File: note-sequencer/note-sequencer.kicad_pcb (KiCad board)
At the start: 2 copper layers, 160.9 x 383.9 mm, 132 parts, among them J1 Pitch, J10 Gate, J11 Velocity, J12 Clock, J13 LED Socket, J14 Conn_01x06_Pin, J2 Gate, J3 Power, J4 Power, J5 Power, J6 Conn_01x06_Socket, J7 Velocity, J8 Clock, J9 Pitch, SW1 SW_DIP_x01, SW10 C#1, SW11 D#1, SW12 F#1, SW13 G#1, SW14 A#1, SW15 C1, SW16 D1, SW17 F1, SW18 E1, SW19 G1, SW2 SW_DIP_x01, SW20 A1, SW21 B1, SW22 C2, SW23 C#2, SW24 D#2, SW25 F#2, SW26 G#2, SW27 A#2, SW28 C2, SW29 D2, SW3 X1, SW30 E2, SW31 F2, SW32 G2, SW33 A2, SW34 B2, SW35 C3, SW4 X2, SW5 X4, SW6 X3, SW7 RotaryEncoder_Switch, SW8 Mode, SW9 Clock Source, U1 TL072

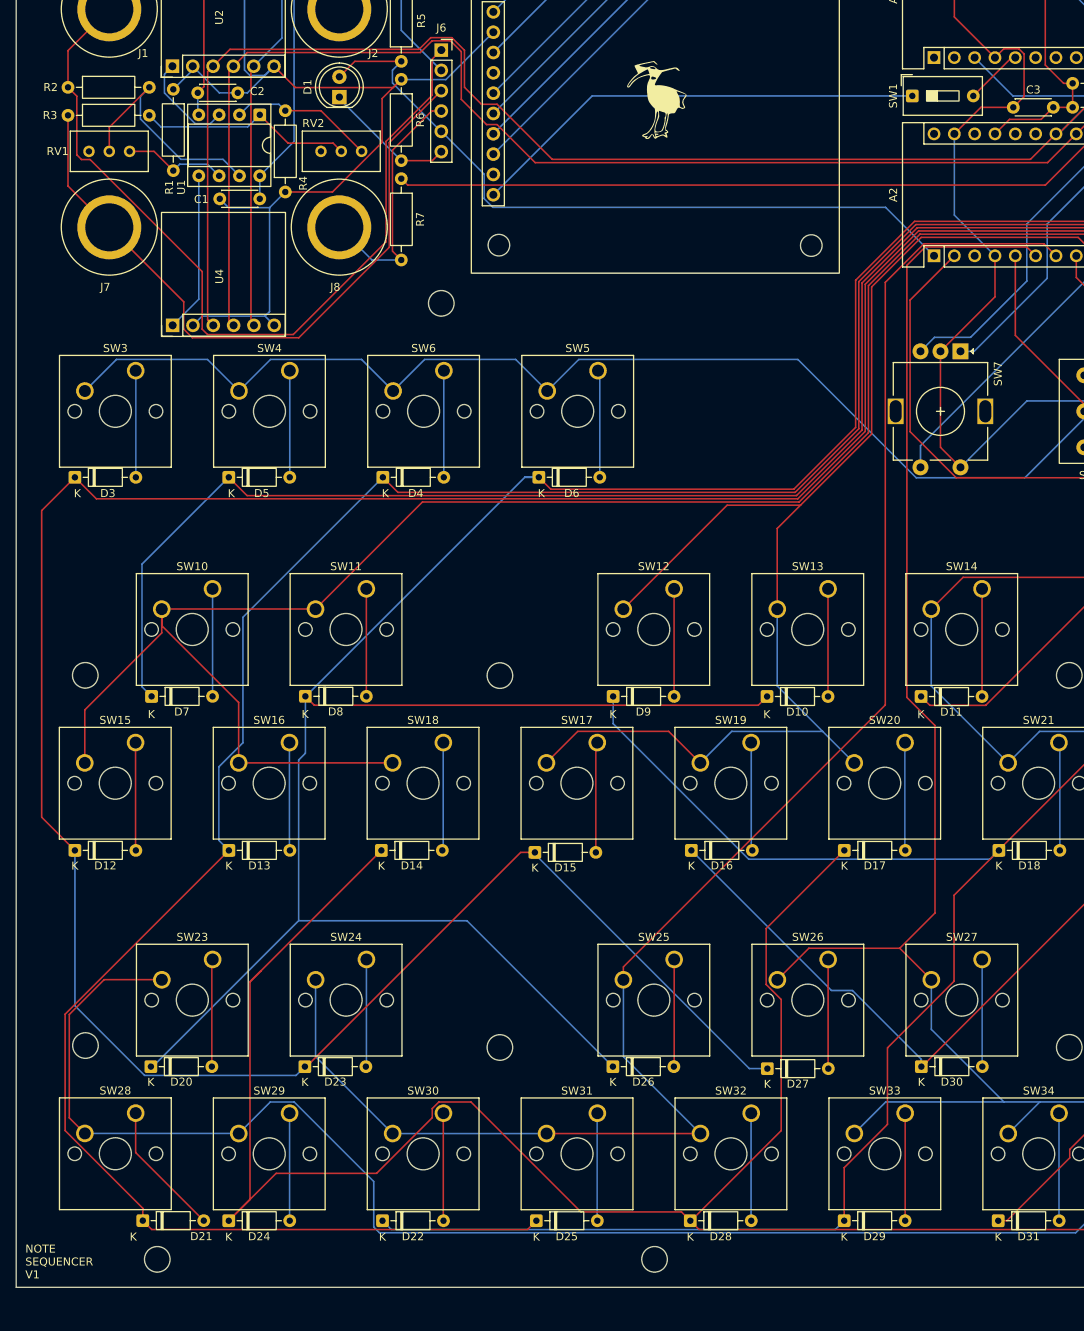
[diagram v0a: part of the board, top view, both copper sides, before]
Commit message: Fix pwm pin controlling screen brightness
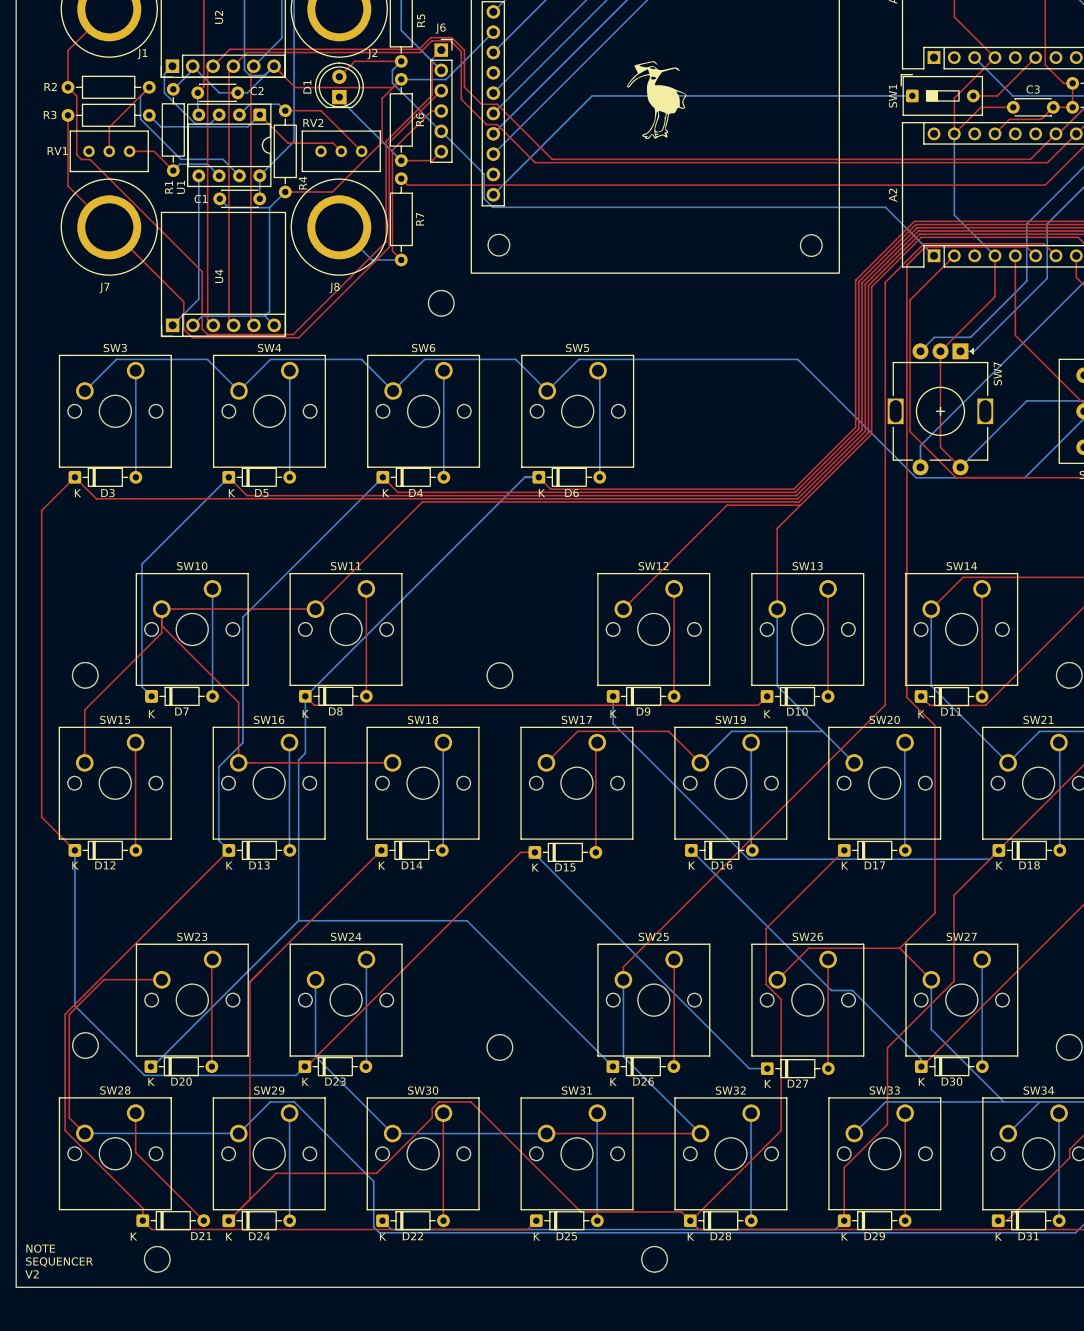
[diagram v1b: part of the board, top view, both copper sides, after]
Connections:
- A1 pad 5: Net-(A1-D2) -> unconnected-(A1-D2-Pad5)
- A1 pad 6: unconnected-(A1-D3-Pad6) -> Net-(A1-D3)
- SW1 pad 2: Net-(A1-D2) -> Net-(A1-D3)
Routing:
- net Net-(A1-D3): track 0.00 -> 9.77 mm
- net Net-(A1-D2): track 7.23 -> 0.00 mm
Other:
- board text added: "NOTE SEQUENCER V2"
- board text removed: "NOTE SEQUENCER V1"
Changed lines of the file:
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@@
 	(net 11 "unconnected-(A1-A0-Pad19)")
 	(net 12 "unconnected-(A1-A1-Pad20)")
-	(net 13 "Net-(A1-D2)")
+	(net 13 "unconnected-(A1-D2-Pad5)")
 	(net 14 "Net-(A1-D10)")
 	(net 15 "unconnected-(A1-D1{slash}TX-Pad1)")
@@
 	(net 51 "Net-(D29-A)")
 	(net 52 "Net-(D30-A)")
-	(net 53 "unconnected-(A1-D3-Pad6)")
+	(net 53 "Net-(A1-D3)")
 	(net 54 "unconnected-(A1-D4-Pad7)")
 	(net 55 "unconnected-(A1-D6-Pad9)")
@@
 			(layers "*.Cu" "*.Mask")
 			(remove_unused_layers no)
-			(net 13 "Net-(A1-D2)")
+			(net 53 "Net-(A1-D3)")
 			(pintype "passive")
 		)
@@
 			(layers "*.Cu" "*.Mask")
 			(remove_unused_layers no)
-			(net 13 "Net-(A1-D2)")
+			(net 13 "unconnected-(A1-D2-Pad5)")
 			(pinfunction "D2")
-			(pintype "bidirectional")
+			(pintype "bidirectional+no_connect")
 		)
 		(pad "6" thru_hole oval
@@
 			(layers "*.Cu" "*.Mask")
 			(remove_unused_layers no)
-			(net 53 "unconnected-(A1-D3-Pad6)")
+			(net 53 "Net-(A1-D3)")
 			(pinfunction "D3")
-			(pintype "bidirectional+no_connect")
+			(pintype "bidirectional")
 		)
 		(pad "7" thru_hole oval
@@
 		(layer "Edge.Cuts")
 	)
-	(gr_text "NOTE\nSEQUENCER\nV1"
+	(gr_text "NOTE\nSEQUENCER\nV2"
 		(at 17 196.5 0)
 		(layer "F.SilkS")
@@
 	)
 	(segment
-		(start 139.311 42.683)
-		(end 141.20605 42.683)
-		(width 0.2)
-		(layer "F.Cu")
-		(net 8)
-	)
-	(segment
 		(start 133.13 38.704)
 		(end 138.21 43.784)
@@
 	)
 	(segment
-		(start 141.20605 42.683)
-		(end 141.851 43.32795)
+		(start 138.21 43.784)
+		(end 133.134126 48.859874)
 		(width 0.2)
 		(layer "F.Cu")
@@
 	)
 	(segment
-		(start 138.21 43.784)
-		(end 139.311 42.683)
-		(width 0.2)
-		(layer "F.Cu")
-		(net 8)
-	)
-	(segment
 		(start 133.13 28.544)
 		(end 133.13 38.704)
@@
 	)
 	(segment
+		(start 133.134126 48.859874)
+		(end 133.134126 53.31772)
+		(width 0.2)
+		(layer "F.Cu")
+		(net 8)
+	)
+	(segment
 		(start 49.5 60.58)
 		(end 55.403913 60.58)
@@
 	)
 	(segment
-		(start 141.851 48.649)
-		(end 140.5 50)
-		(width 0.2)
-		(layer "F.Cu")
-		(net 8)
-	)
-	(segment
 		(start 136.451846 50)
 		(end 133.134126 53.31772)
@@
 	)
 	(segment
-		(start 141.851 43.32795)
-		(end 141.851 48.649)
-		(width 0.2)
-		(layer "F.Cu")
-		(net 8)
-	)
-	(segment
 		(start 62.978647 47.521353)
 		(end 50.751923 47.521353)
@@
 	)
 	(segment
-		(start 140.290973 43.784)
-		(end 140.75 43.784)
-		(width 0.2)
-		(layer "F.Cu")
-		(net 13)
-	)
-	(segment
-		(start 135.5 48.574973)
-		(end 140.290973 43.784)
-		(width 0.2)
-		(layer "F.Cu")
-		(net 13)
-	)
-	(segment
 		(start 91.724898 34.549562)
 		(end 151.835562 34.549562)
@@
 	)
 	(segment
-		(start 144.5 44.71137)
-		(end 144.5 34.834)
+		(start 144.5 34.834)
+		(end 138.21 28.544)
 		(width 0.2)
 		(layer "F.Cu")
@@
 	)
 	(segment
-		(start 138.21 28.544)
-		(end 138.21 28.29)
+		(start 147.92 47)
+		(end 146.78863 47)
 		(width 0.2)
 		(layer "F.Cu")
@@
 	)
 	(segment
-		(start 45.58 77.25)
-		(end 45.209 76.879)
+		(start 138.21 28.544)
+		(end 138.21 28.29)
 		(width 0.2)
 		(layer "F.Cu")
@@
 	)
 	(segment
-		(start 147.92 47)
-		(end 146.78863 47)
+		(start 45.58 77.25)
+		(end 45.209 76.879)
 		(width 0.2)
 		(layer "F.Cu")
@@
 	)
 	(segment
-		(start 140.031846 51.5)
-		(end 138.214126 53.31772)
+		(start 146.78863 47)
+		(end 144.5 44.71137)
 		(width 0.2)
 		(layer "F.Cu")
@@
 	)
 	(segment
-		(start 144.5 34.834)
-		(end 138.21 28.544)
+		(start 140.031846 51.5)
+		(end 138.214126 53.31772)
 		(width 0.2)
 		(layer "F.Cu")
@@
 	)
 	(segment
-		(start 144 51.5)
-		(end 140.031846 51.5)
+		(start 144.5 44.71137)
+		(end 144.5 34.834)
 		(width 0.2)
 		(layer "F.Cu")
@@
 	)
 	(segment
-		(start 146.78863 47)
-		(end 144.5 44.71137)
+		(start 144 51.5)
+		(end 140.031846 51.5)
 		(width 0.2)
 		(layer "F.Cu")
@@
 	)
 	(segment
+		(start 138.499027 48.574973)
+		(end 143.29 43.784)
+		(width 0.2)
+		(layer "F.Cu")
+		(net 53)
+	)
+	(segment
+		(start 135.5 48.574973)
+		(end 138.499027 48.574973)
+		(width 0.2)
+		(layer "F.Cu")
+		(net 53)
+	)
+	(segment

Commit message: Update some designs
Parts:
- removed F0, F1, F2, F3: foot, modular2:foot
- moved REF** 17.3 mm to (17.8, 393.0)
- moved REF** 17.1 mm to (16.8, 190.5)
- moved SW7 15.9 mm to (118.4, 77.0)
- moved D21 12.8 mm to (19.4, 185.6)
- moved REF** 10.1 mm to (167.0, 190.5)
- moved REF** 8.99 mm to (168.0, 393.0)
- moved A1 5.13 mm to (126.8, 40.3)
- moved C1 5.13 mm to (37.6, 57.9)
- moved C2 5.13 mm to (39.8, 44.7)
- moved C3 5.13 mm to (136.8, 46.5)
- moved D1 5.13 mm to (52.5, 45.2)
- moved D10 5.13 mm to (106.0, 120.1)
- moved D11 5.13 mm to (125.2, 120.1)
- moved D12 5.13 mm to (19.5, 139.4)
- moved D13 5.13 mm to (38.7, 139.4)
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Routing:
- net GND: track 378.1 -> 402.5 mm
- net Net-(A2-A2): track 40.0 -> 60.5 mm
- net Net-(A2-D2): track 170.2 -> 156.5 mm
- net Net-(A2-D11): track 450.2 -> 438.2 mm
- net Net-(A2-D9): track 438.9 -> 428.1 mm
- net Net-(A2-D7): track 216.3 -> 205.5 mm
- net Net-(A2-D8): track 425.6 -> 414.9 mm
- net Net-(A2-A1): track 37.3 -> 47.7 mm
- net Net-(A2-A0): track 54.0 -> 62.7 mm
- net Net-(A2-D12): track 387.0 -> 393.1 mm
- net Net-(A2-D10): track 454.3 -> 449.1 mm
- net Net-(A2-D6): track 167.0 -> 162.6 mm
- net Net-(D21-A): track 17.0 -> 13.3 mm
- net Net-(D32-A): track 16.0 -> 13.4 mm
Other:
- board size 160.9 x 383.9 mm -> 160.4 x 386.8 mm
